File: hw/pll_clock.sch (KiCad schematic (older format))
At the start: 22 parts, among them J7 BNC, J8 BNC, U7 5P49V5925, Y1 25MHz

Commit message: several updates...
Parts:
- removed J8: BNC, proj_footprints:BNC_Molex_0731713150, symbol Connector:Conn_Coaxial
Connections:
- net ADC_CLK: now reaches R28.1
- net at Y1.1: now also U7.4 (XIN/REF); no longer U7.3 (XOUT)
- net at Y1.3: now also U7.3 (XOUT); no longer U7.4 (XIN/REF)
- net at R27.2: now also U7.20 (OUT1); no longer U7.14 (OUT3)
- net at R28.2: now also U7.17 (OUT2); no longer U7.11 (OUT4)
- net at R26.2: now also U7.11 (OUT4); no longer U7.20 (OUT1)
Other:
- moved on the sheet: C49, J7, R26, R27, R28
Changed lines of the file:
@@
 $Descr A4 11693 8268
 encoding utf-8
-Sheet 4 4
+Sheet 4 5
 Title ""
 Date ""
@@
 NoConn ~ 5100 3900
 NoConn ~ 5100 3400
-NoConn ~ 6100 3200
 NoConn ~ 5100 3100
 NoConn ~ 5100 3200
@@
 F 5 "Abracon" V 4700 2800 50  0001 C CNN "Manufacturer"
 	1    4700 2800
-	0    1    1    0
+	0    1    -1   0
 $EndComp
 Wire Wire Line
@@
 Wire Wire Line
 	4500 3700 4650 3700
-Text GLabel 6950 2900 2    50   Output ~ 0
+Text GLabel 6950 3800 2    50   Output ~ 0
 FPGA_CLK
 Wire Wire Line
-	6100 2900 6350 2900
+	6100 3800 6350 3800
 $Comp
 L Device:R_Small R?
@@
 L Device:R_Small R?
 U 1 1 60D6AA6F
-P 6450 2900
+P 6450 3800
 AR Path="/60AABC24/60D6AA6F" Ref="R?"  Part="1"
 AR Path="/60B16D71/60D6AA6F" Ref="R26"  Part="1"
-F 0 "R26" V 6350 2900 50  0000 C CNN
-F 1 "33" V 6550 2900 50  0000 C CNN
-F 2 "Resistor_SMD:R_0603_1608Metric" H 6450 2900 50  0001 C CNN
-F 3 "~" H 6450 2900 50  0001 C CNN
-F 4 " RC0603FR-0733RL " V 6450 2900 50  0001 C CNN "Part"
-F 5 "Yageo" V 6450 2900 50  0001 C CNN "Manufacturer"
-	1    6450 2900
+F 0 "R26" V 6350 3800 50  0000 C CNN
+F 1 "33" V 6550 3800 50  0000 C CNN
+F 2 "Resistor_SMD:R_0603_1608Metric" H 6450 3800 50  0001 C CNN
+F 3 "~" H 6450 3800 50  0001 C CNN
+F 4 " RC0603FR-0733RL " V 6450 3800 50  0001 C CNN "Part"
+F 5 "Yageo" V 6450 3800 50  0001 C CNN "Manufacturer"
+	1    6450 3800
 	0    1    1    0
 $EndComp
 Wire Wire Line
-	6550 2900 6950 2900
+	6550 3800 6950 3800
 $Comp
 L fmc:100nF_603 C?
@@
 	5000 2050 5300 2050
 Wire Wire Line
-	6100 3500 6350 3500
-Wire Wire Line
-	6100 3800 6350 3800
-$Comp
-L Connector:Conn_Coaxial J8
-U 1 1 6092C0EF
-P 7300 3800
-F 0 "J8" H 7400 3775 50  0000 L CNN
-F 1 "BNC" H 7400 3684 50  0000 L CNN
-F 2 "proj_footprints:BNC_Molex_0731713150" H 7300 3800 50  0001 C CNN
-F 3 " ~" H 7300 3800 50  0001 C CNN
-F 4 "0731713150" H 7300 3800 50  0001 C CNN "Part"
-F 5 "Molex" H 7300 3800 50  0001 C CNN "Manufacturer"
-	1    7300 3800
-	1    0    0    -1
-$EndComp
-Wire Wire Line
-	6550 3800 7100 3800
-Wire Wire Line
-	7300 3700 7050 3700
-Wire Wire Line
-	7050 3700 7050 4000
-Wire Wire Line
-	7050 4000 7300 4000
+	6100 2900 6350 2900
+Wire Wire Line
+	6100 3200 6350 3200
 $Comp
 L power:GND #PWR?
 U 1 1 6092DB98
-P 7050 4000
+P 7900 3200
 AR Path="/6086F2E3/6092DB98" Ref="#PWR?"  Part="1"
 AR Path="/60AABC24/6092DB98" Ref="#PWR?"  Part="1"
 AR Path="/60B16D71/6092DB98" Ref="#PWR?"  Part="1"
-F 0 "#PWR?" H 7050 3750 50  0001 C CNN
-F 1 "GND" H 7055 3827 50  0000 C CNN
-F 2 "" H 7050 4000 50  0001 C CNN
-F 3 "" H 7050 4000 50  0001 C CNN
-	1    7050 4000
-	1    0    0    -1
-$EndComp
-Connection ~ 7050 4000
+F 0 "#PWR?" H 7900 2950 50  0001 C CNN
+F 1 "GND" H 7905 3027 50  0000 C CNN
+F 2 "" H 7900 3200 50  0001 C CNN
+F 3 "" H 7900 3200 50  0001 C CNN
+	1    7900 3200
+	1    0    0    -1
+$EndComp
 $Comp
 L fmc:100nF_603 C?
@@
 L Device:R_Small R?
 U 1 1 60C371EA
-P 6450 3500
+P 6450 2900
 AR Path="/60AABC24/60C371EA" Ref="R?"  Part="1"
 AR Path="/60B16D71/60C371EA" Ref="R27"  Part="1"
-F 0 "R27" V 6350 3500 50  0000 C CNN
-F 1 "33" V 6550 3500 50  0000 C CNN
-F 2 "Resistor_SMD:R_0603_1608Metric" H 6450 3500 50  0001 C CNN
-F 3 "~" H 6450 3500 50  0001 C CNN
-F 4 " RC0603FR-0733RL " V 6450 3500 50  0001 C CNN "Part"
-F 5 "Yageo" V 6450 3500 50  0001 C CNN "Manufacturer"
-	1    6450 3500
+F 0 "R27" V 6350 2900 50  0000 C CNN
+F 1 "33" V 6550 2900 50  0000 C CNN
+F 2 "Resistor_SMD:R_0603_1608Metric" H 6450 2900 50  0001 C CNN
+F 3 "~" H 6450 2900 50  0001 C CNN
+F 4 " RC0603FR-0733RL " V 6450 2900 50  0001 C CNN "Part"
+F 5 "Yageo" V 6450 2900 50  0001 C CNN "Manufacturer"
+	1    6450 2900
 	0    1    1    0
 $EndComp
@@
 L Device:R_Small R?
 U 1 1 60C375F6
-P 6450 3800
+P 6450 3200
 AR Path="/60AABC24/60C375F6" Ref="R?"  Part="1"
 AR Path="/60B16D71/60C375F6" Ref="R28"  Part="1"
-F 0 "R28" V 6350 3800 50  0000 C CNN
-F 1 "33" V 6550 3800 50  0000 C CNN
-F 2 "Resistor_SMD:R_0603_1608Metric" H 6450 3800 50  0001 C CNN
-F 3 "~" H 6450 3800 50  0001 C CNN
-F 4 " RC0603FR-0733RL " V 6450 3800 50  0001 C CNN "Part"
-F 5 "Yageo" V 6450 3800 50  0001 C CNN "Manufacturer"
-	1    6450 3800
+F 0 "R28" V 6350 3200 50  0000 C CNN
+F 1 "33" V 6550 3200 50  0000 C CNN
+F 2 "Resistor_SMD:R_0603_1608Metric" H 6450 3200 50  0001 C CNN
+F 3 "~" H 6450 3200 50  0001 C CNN
+F 4 " RC0603FR-0733RL " V 6450 3200 50  0001 C CNN "Part"
+F 5 "Yageo" V 6450 3200 50  0001 C CNN "Manufacturer"
+	1    6450 3200
 	0    1    1    0
 $EndComp
@@
 L Connector:Conn_Coaxial J7
 U 1 1 60C731B4
-P 7300 3500
-F 0 "J7" H 7400 3475 50  0000 L CNN
-F 1 "BNC" H 7400 3384 50  0000 L CNN
-F 2 "proj_footprints:BNC_Molex_0731713150" H 7300 3500 50  0001 C CNN
-F 3 " ~" H 7300 3500 50  0001 C CNN
-F 4 "0731713150" H 7300 3500 50  0001 C CNN "Part"
-F 5 "Molex" H 7300 3500 50  0001 C CNN "Manufacturer"
-	1    7300 3500
+P 7900 2900
+F 0 "J7" H 8000 2875 50  0000 L CNN
+F 1 "BNC" H 8000 2784 50  0000 L CNN
+F 2 "proj_footprints:BNC_Molex_0731713150" H 7900 2900 50  0001 C CNN
+F 3 " ~" H 7900 2900 50  0001 C CNN
+F 4 "0731713150" H 7900 2900 50  0001 C CNN "Part"
+F 5 "Molex" H 7900 2900 50  0001 C CNN "Manufacturer"
+	1    7900 2900
 	1    0    0    -1
 $EndComp
@@
 L fmc:100nF_603 C?
 U 1 1 60B85B4A
-P 6800 3500
+P 7400 2900
 AR Path="/6086F2E3/60B85B4A" Ref="C?"  Part="1"
 AR Path="/60B16D71/60B85B4A" Ref="C49"  Part="1"
-F 0 "C49" V 6950 3500 50  0000 C CNN
-F 1 "100n" V 6650 3500 50  0000 C CNN
-F 2 "Capacitor_SMD:C_0603_1608Metric" H 6838 3350 50  0001 C CNN
-F 3 "~" H 6800 3500 50  0001 C CNN
-F 4 "GCJ188R71E104KA12D" H 6925 3700 50  0001 C CNN "Part"
-F 5 "Murata" H 7025 3800 50  0001 C CNN "Manufacturer"
-	1    6800 3500
+F 0 "C49" V 7550 2900 50  0000 C CNN
+F 1 "100n" V 7250 2900 50  0000 C CNN
+F 2 "Capacitor_SMD:C_0603_1608Metric" H 7438 2750 50  0001 C CNN
+F 3 "~" H 7400 2900 50  0001 C CNN
+F 4 "GCJ188R71E104KA12D" H 7525 3100 50  0001 C CNN "Part"
+F 5 "Murata" H 7625 3200 50  0001 C CNN "Manufacturer"
+	1    7400 2900
 	0    -1   -1   0
 $EndComp
 Wire Wire Line
-	6950 3500 7100 3500
-Wire Wire Line
-	6550 3500 6650 3500
+	7550 2900 7700 2900
 Wire Wire Line
 	5500 2200 5600 2200
@@
 Wire Wire Line
 	5800 2200 5900 2200
+NoConn ~ 6100 3500
+Text GLabel 6950 3200 2    50   Output ~ 0
+ADC_CLK
+Wire Wire Line
+	6550 3200 6950 3200
+Wire Wire Line
+	6550 2900 7250 2900
+Wire Wire Line
+	7900 3100 7900 3200
 $EndSCHEMATC

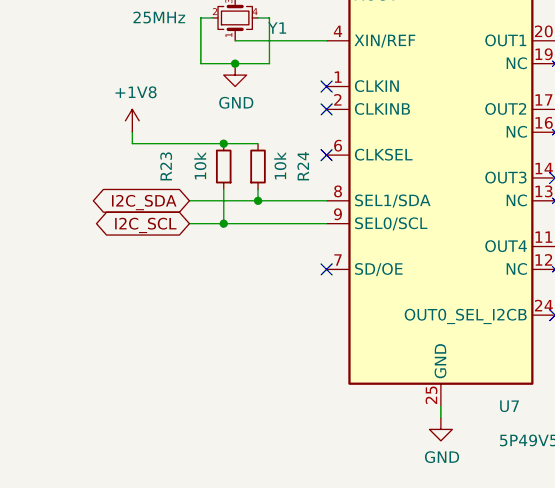
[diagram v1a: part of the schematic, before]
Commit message: Started to work on analog front-end; ADC connected to fpga
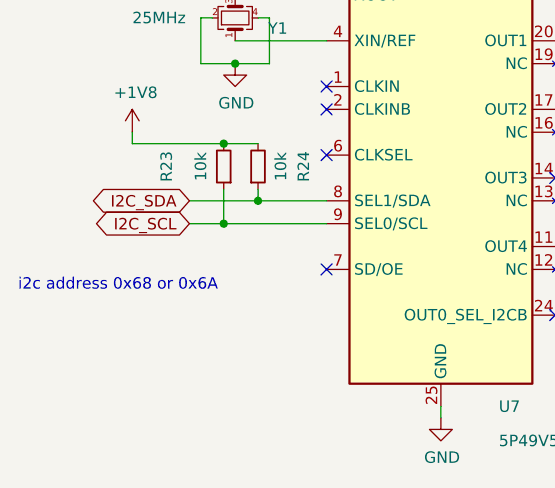
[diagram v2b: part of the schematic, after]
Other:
- note added: "i2c address 0x68 or 0x6A"
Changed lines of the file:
@@
 $Descr A4 11693 8268
 encoding utf-8
-Sheet 4 5
+Sheet 4 7
 Title ""
 Date ""
@@
 Wire Wire Line
 	7900 3100 7900 3200
+Text Notes 3750 4000 0    50   ~ 0
+i2c address 0x68 or 0x6A
 $EndSCHEMATC

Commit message: more work (don't recall details :-()
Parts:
- removed C49: 100n, Capacitor_SMD:C_0603_1608Metric, symbol fmc:100nF_603
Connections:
- net at R27.1: now also J7.1 (In)
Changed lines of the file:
@@
 	1    0    0    -1
 $EndComp
-$Comp
-L fmc:100nF_603 C?
-U 1 1 60B85B4A
-P 7400 2900
-AR Path="/6086F2E3/60B85B4A" Ref="C?"  Part="1"
-AR Path="/60B16D71/60B85B4A" Ref="C49"  Part="1"
-F 0 "C49" V 7550 2900 50  0000 C CNN
-F 1 "100n" V 7250 2900 50  0000 C CNN
-F 2 "Capacitor_SMD:C_0603_1608Metric" H 7438 2750 50  0001 C CNN
-F 3 "~" H 7400 2900 50  0001 C CNN
-F 4 "GCJ188R71E104KA12D" H 7525 3100 50  0001 C CNN "Part"
-F 5 "Murata" H 7625 3200 50  0001 C CNN "Manufacturer"
-	1    7400 2900
-	0    -1   -1   0
-$EndComp
-Wire Wire Line
-	7550 2900 7700 2900
 Wire Wire Line
 	5500 2200 5600 2200
@@
 	6550 3200 6950 3200
 Wire Wire Line
-	6550 2900 7250 2900
-Wire Wire Line
 	7900 3100 7900 3200
 Text Notes 3750 4000 0    50   ~ 0
 i2c address 0x68 or 0x6A
+Wire Wire Line
+	6550 2900 7700 2900
 $EndSCHEMATC

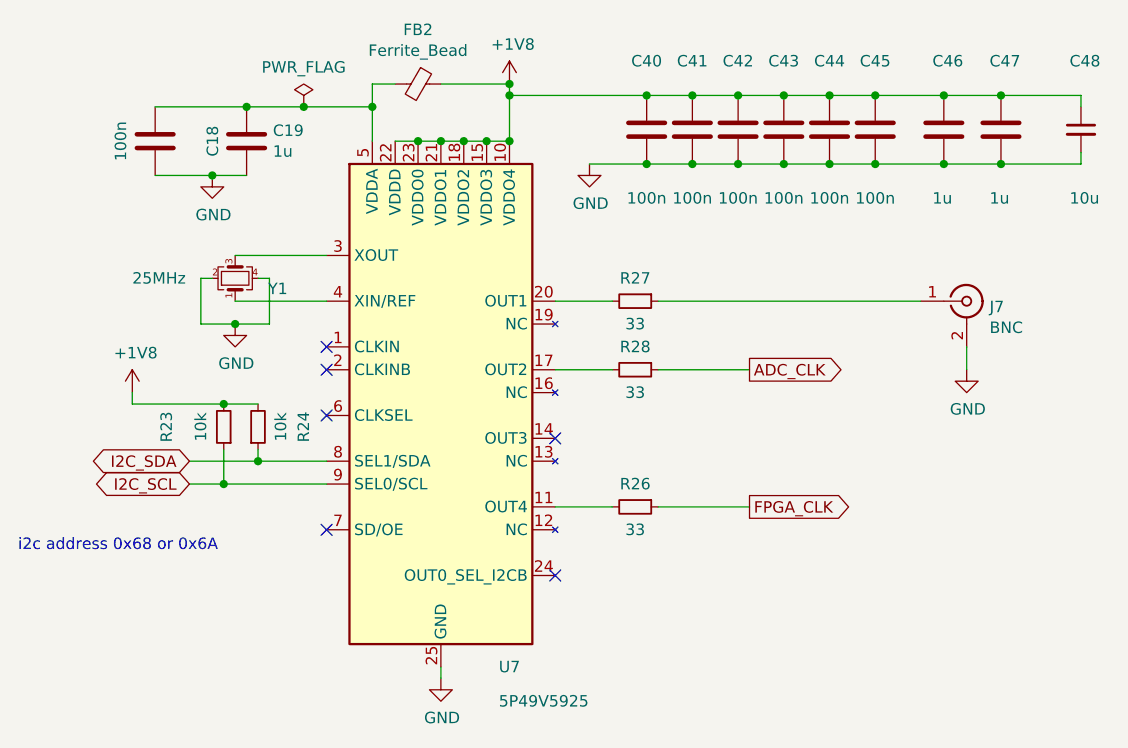
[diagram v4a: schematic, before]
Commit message: everything hooked up + layed out; 0.2/0.4mm vias :-(
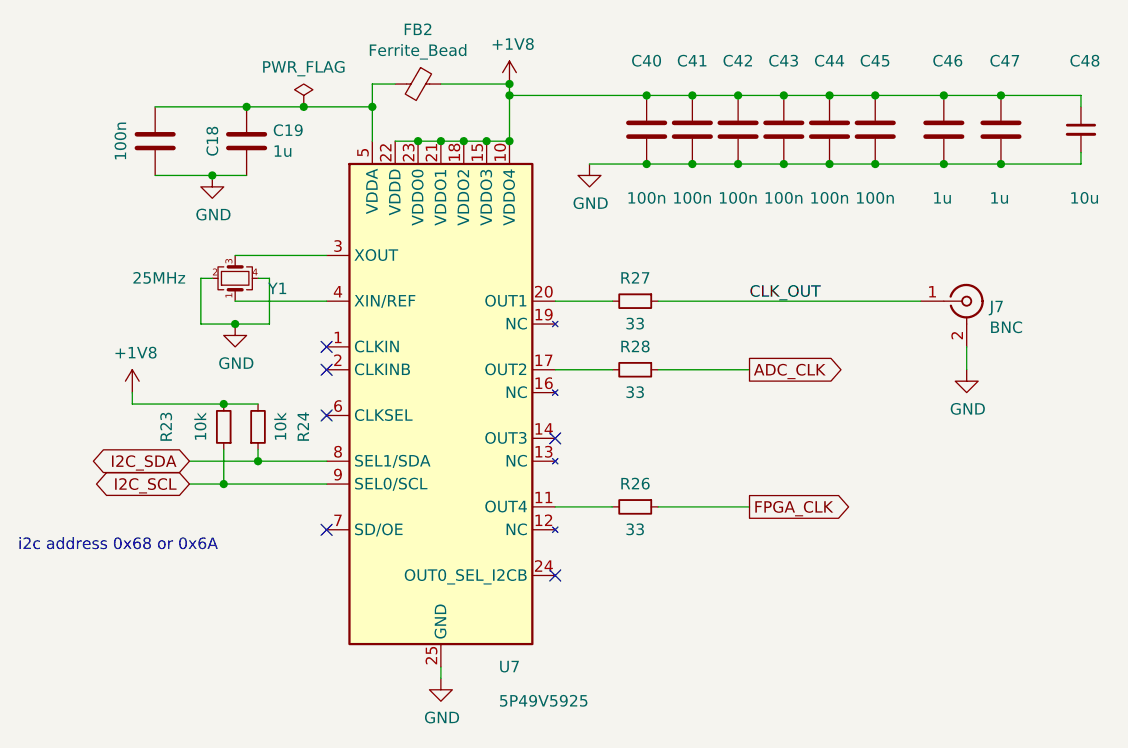
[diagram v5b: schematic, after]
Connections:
- net CLK_OUT: now reaches J7.1 (In), R27.1
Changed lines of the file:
@@
 $Descr A4 11693 8268
 encoding utf-8
-Sheet 4 8
+Sheet 5 9
 Title ""
 Date ""
@@
 Wire Wire Line
 	6550 2900 7700 2900
+Text Label 6950 2900 0    50   ~ 0
+CLK_OUT
 $EndSCHEMATC

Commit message: prototype version
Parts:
- added TP2: Ref, proj_footprints:TestPoint_Pad_D0.8mm_no_CY, symbol Connector:TestPoint
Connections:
- net at U7.24 (OUT0_SEL_I2CB): now also TP2.1
- no-connect marks 6 -> 5
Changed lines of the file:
@@
 Wire Wire Line
 	5900 2200 5900 2000
-NoConn ~ 6100 4100
 NoConn ~ 5100 3900
 NoConn ~ 5100 3400
@@
 	0    1    1    0
 $EndComp
+$Comp
+L Connector:Conn_Coaxial J7
+U 1 1 60C731B4
+P 7900 2900
+F 0 "J7" H 8000 2875 50  0000 L CNN
+F 1 "BNC" H 8000 2784 50  0000 L CNN
+F 2 "proj_footprints:BNC_Molex_0731713150" H 7900 2900 50  0001 C CNN
+F 3 " ~" H 7900 2900 50  0001 C CNN
+F 4 "0731713150" H 7900 2900 50  0001 C CNN "Part"
+F 5 "Molex" H 7900 2900 50  0001 C CNN "Manufacturer"
+	1    7900 2900
+	1    0    0    -1
+$EndComp
+NoConn ~ 6100 3500
+Text GLabel 6950 3200 2    50   Output ~ 0
+ADC_CLK
+Wire Wire Line
+	6550 3200 6950 3200
+Wire Wire Line
+	7900 3100 7900 3200
+Text Notes 3750 4000 0    50   ~ 0
+i2c address 0x68 or 0x6A
+Wire Wire Line
+	6550 2900 7700 2900
+Text Label 6950 2900 0    50   ~ 0
+CLK_OUT
 Wire Wire Line
 	5400 2200 5500 2200
+Connection ~ 5500 2200
+Wire Wire Line
+	5500 2200 5600 2200
+Connection ~ 5600 2200
+Wire Wire Line
+	5600 2200 5700 2200
+Connection ~ 5700 2200
+Wire Wire Line
+	5700 2200 5800 2200
+Wire Wire Line
+	5800 2200 5900 2200
+Connection ~ 5800 2200
+Connection ~ 5900 2200
 $Comp
 L fmc:5P49V5925 U7
@@
 $EndComp
 $Comp
-L Connector:Conn_Coaxial J7
-U 1 1 60C731B4
-P 7900 2900
-F 0 "J7" H 8000 2875 50  0000 L CNN
-F 1 "BNC" H 8000 2784 50  0000 L CNN
-F 2 "proj_footprints:BNC_Molex_0731713150" H 7900 2900 50  0001 C CNN
-F 3 " ~" H 7900 2900 50  0001 C CNN
-F 4 "0731713150" H 7900 2900 50  0001 C CNN "Part"
-F 5 "Molex" H 7900 2900 50  0001 C CNN "Manufacturer"
-	1    7900 2900
-	1    0    0    -1
-$EndComp
-Wire Wire Line
-	5500 2200 5600 2200
-Connection ~ 5500 2200
-Connection ~ 5900 2200
-Connection ~ 5600 2200
-Wire Wire Line
-	5600 2200 5700 2200
-Connection ~ 5700 2200
-Wire Wire Line
-	5700 2200 5800 2200
-Connection ~ 5800 2200
-Wire Wire Line
-	5800 2200 5900 2200
-NoConn ~ 6100 3500
-Text GLabel 6950 3200 2    50   Output ~ 0
-ADC_CLK
-Wire Wire Line
-	6550 3200 6950 3200
-Wire Wire Line
-	7900 3100 7900 3200
-Text Notes 3750 4000 0    50   ~ 0
-i2c address 0x68 or 0x6A
-Wire Wire Line
-	6550 2900 7700 2900
-Text Label 6950 2900 0    50   ~ 0
-CLK_OUT
+L Connector:TestPoint TP2
+U 1 1 61006520
+P 6950 4100
+F 0 "TP2" V 6904 4288 50  0000 L CNN
+F 1 "Ref" V 6995 4288 50  0000 L CNN
+F 2 "proj_footprints:TestPoint_Pad_D0.8mm_no_CY" H 7150 4100 50  0001 C CNN
+F 3 "~" H 7150 4100 50  0001 C CNN
+	1    6950 4100
+	0    1    1    0
+$EndComp
+Wire Wire Line
+	6100 4100 6950 4100
 $EndSCHEMATC
